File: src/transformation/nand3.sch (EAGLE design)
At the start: 7 parts, among them Q1 BSS92, Q2 BSS92, Q3 BSS97, Q4 BSS97

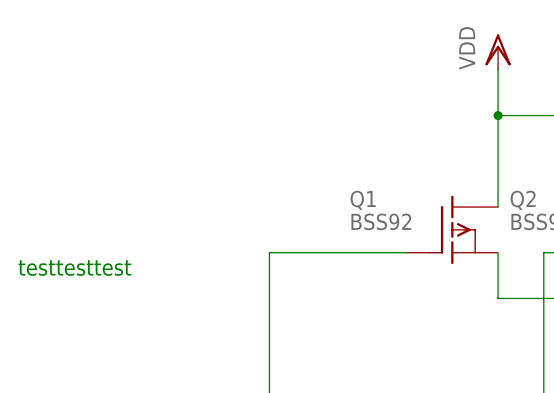
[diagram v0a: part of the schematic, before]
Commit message: moved instance into part to decrease complexity for other metamodels which are in consistency with the eagle metamodel, added a uid for parts
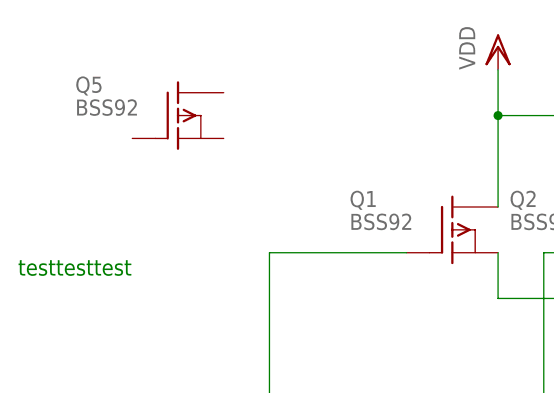
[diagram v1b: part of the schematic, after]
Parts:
- added Q5: BSS92, transistor-fet:BSS92
- Q1: UID (none) -> 2
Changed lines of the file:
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@@
 <attribute name="P1" value="0001"/>
 <attribute name="TEST2" value="5"/>
+<attribute name="UID" value="2"/>
 </part>
 <part name="Q2" library="transistor-fet" deviceset="BSS92" device="">
@@
 <part name="A" library="pinhead" deviceset="PINHD-1X1" device=""/>
 <part name="B" library="pinhead" deviceset="PINHD-1X1" device=""/>
+<part name="Q5" library="transistor-fet" deviceset="BSS92" device="">
+<attribute name="P1" value="0001"/>
+<attribute name="TEST2" value="5"/>
+</part>
 </parts>
 <sheets>
@@
 <attribute name="P1" x="-182.88" y="172.72" size="1.778" layer="96" display="off"/>
 <attribute name="TEST2" x="-182.88" y="172.72" size="1.778" layer="96" display="off"/>
+<attribute name="UID" x="-182.88" y="172.72" size="1.778" layer="96" display="off"/>
 </instance>
 <instance part="Q2" gate="G$1" x="-165.1" y="172.72">
@@
 <instance part="A" gate="G$1" x="-215.9" y="137.16" rot="R180"/>
 <instance part="B" gate="G$1" x="-215.9" y="119.38" rot="R180"/>
+<instance part="Q5" gate="G$1" x="-213.36" y="185.42">
+<attribute name="P1" x="-213.36" y="185.42" size="1.778" layer="96" display="off"/>
+<attribute name="TEST2" x="-213.36" y="185.42" size="1.778" layer="96" display="off"/>
+</instance>
 </instances>
 <busses>
